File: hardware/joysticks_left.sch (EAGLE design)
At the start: 8 parts, among them IC1 MEGA16-M

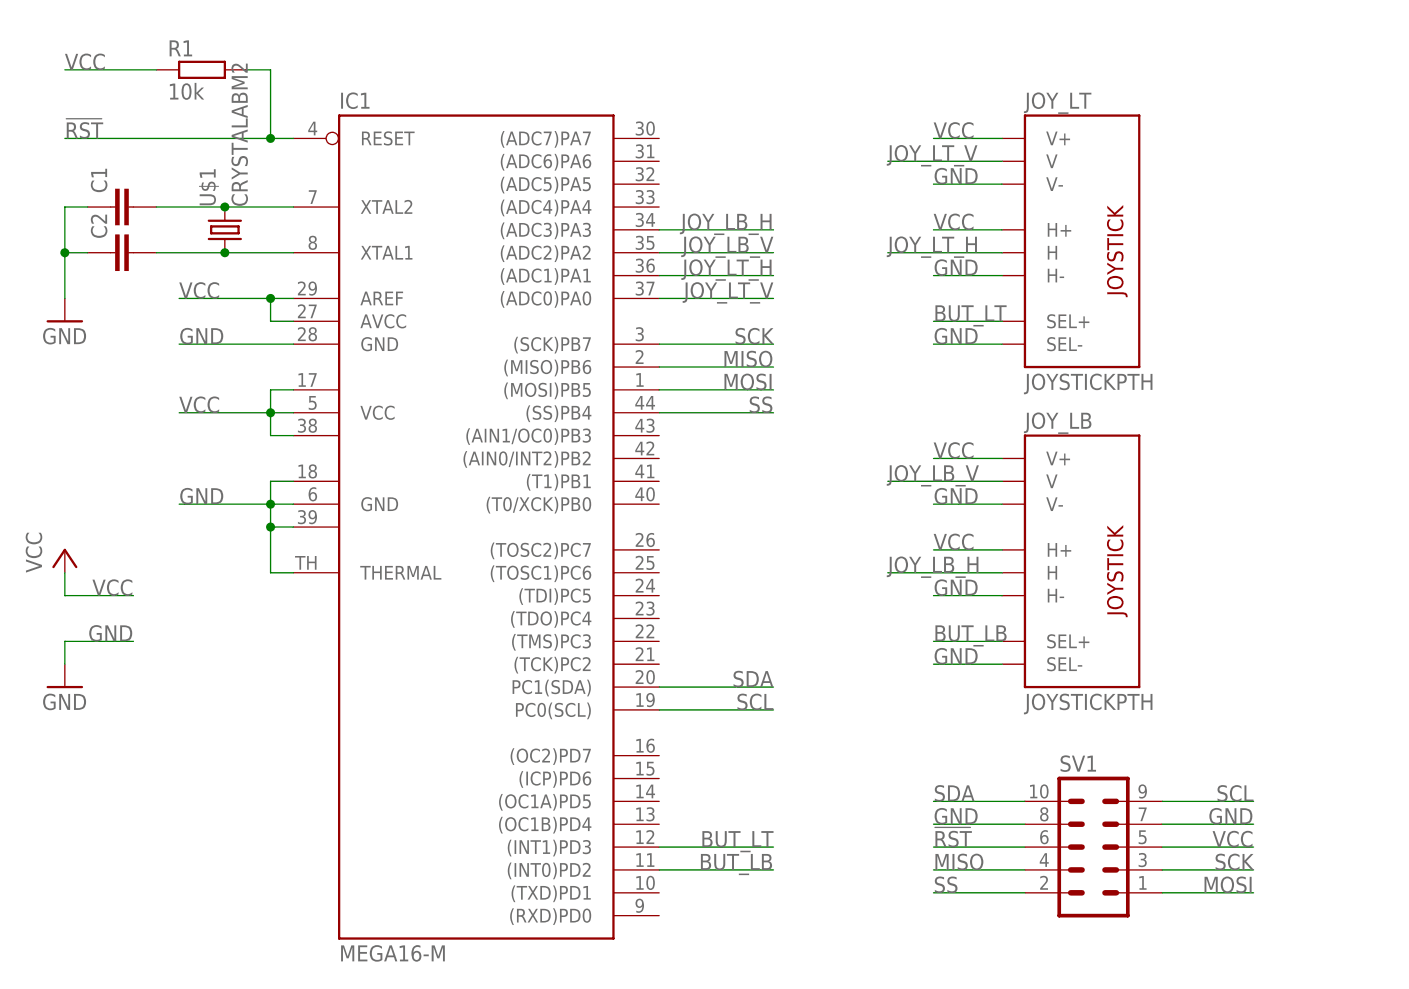
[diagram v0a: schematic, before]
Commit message: added mode selection jumper (SPI/I2C)
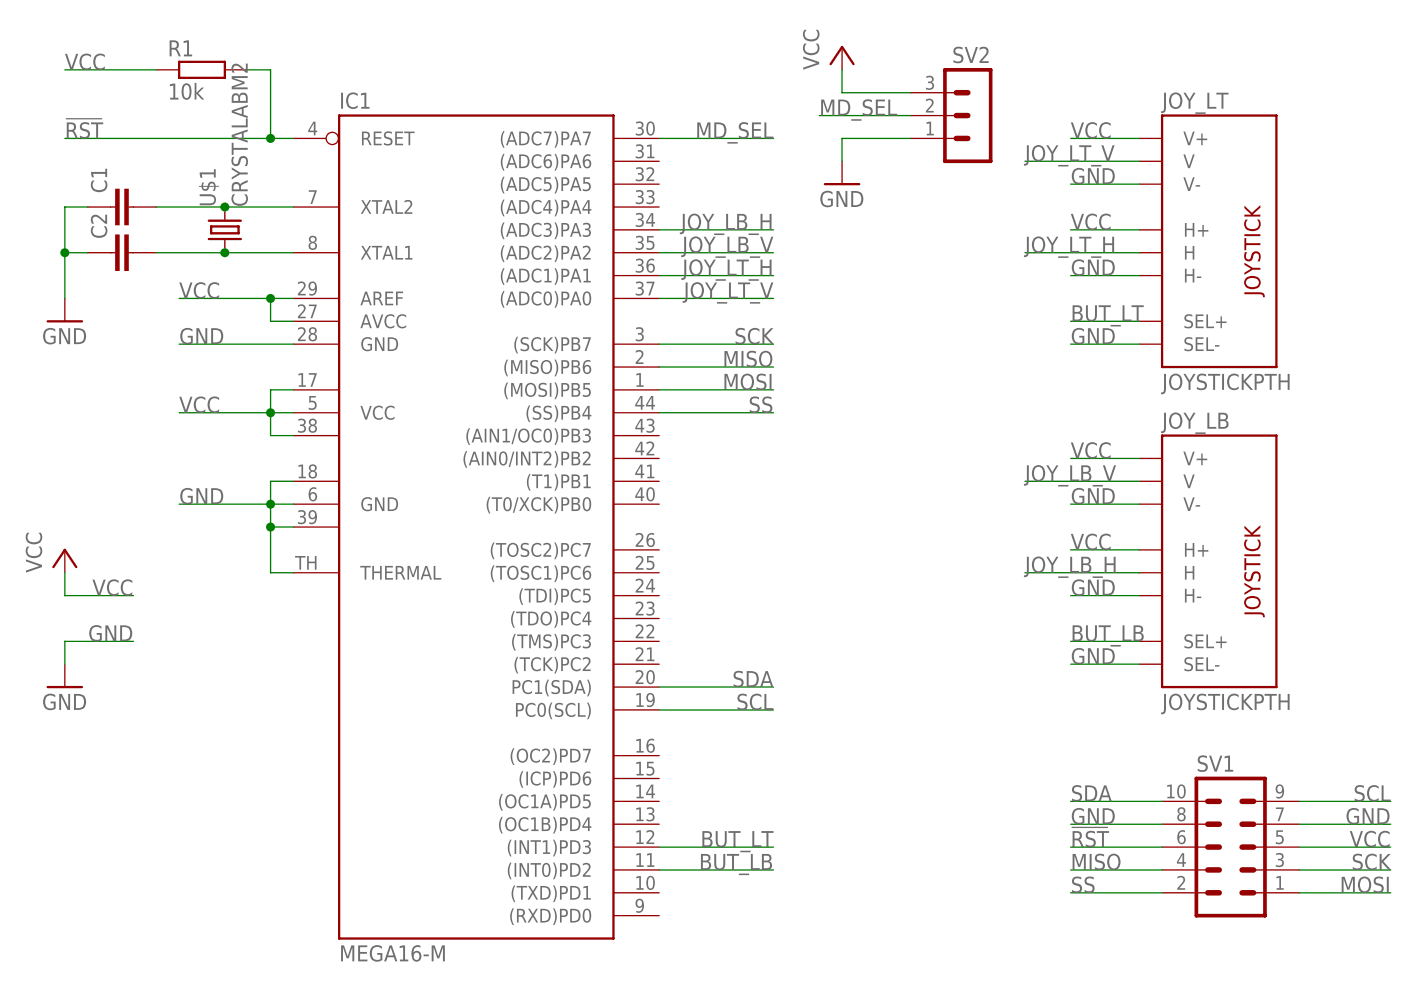
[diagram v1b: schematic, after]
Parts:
- added SV2: (no value), con-lstb:MA03-1
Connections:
- new net MD_SEL: IC1.(ADC7)PA7, SV2.2
- net GND: now also SV2.1
- net VCC: now also SV2.3
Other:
- moved on the sheet: JOY_LB, JOY_LT, SV1

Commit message: set value for xtal-caps
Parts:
- C1, C2: value (none) -> 18p
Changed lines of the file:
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@@
 <part name="P+1" library="supply1" deviceset="VCC" device=""/>
 <part name="U$1" library="jocki" deviceset="CRYSTAL" device="ABM2"/>
-<part name="C1" library="rcl" deviceset="C-EU" device="C0603"/>
-<part name="C2" library="rcl" deviceset="C-EU" device="C0603"/>
+<part name="C1" library="rcl" deviceset="C-EU" device="C0603" value="18p"/>
+<part name="C2" library="rcl" deviceset="C-EU" device="C0603" value="18p"/>
 <part name="GND2" library="supply1" deviceset="GND" device=""/>
 <part name="SV1" library="con-lstb" deviceset="MA05-2" device=""/>
